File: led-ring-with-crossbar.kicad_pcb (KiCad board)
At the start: 2 copper layers, 99 x 99 mm, 88 parts

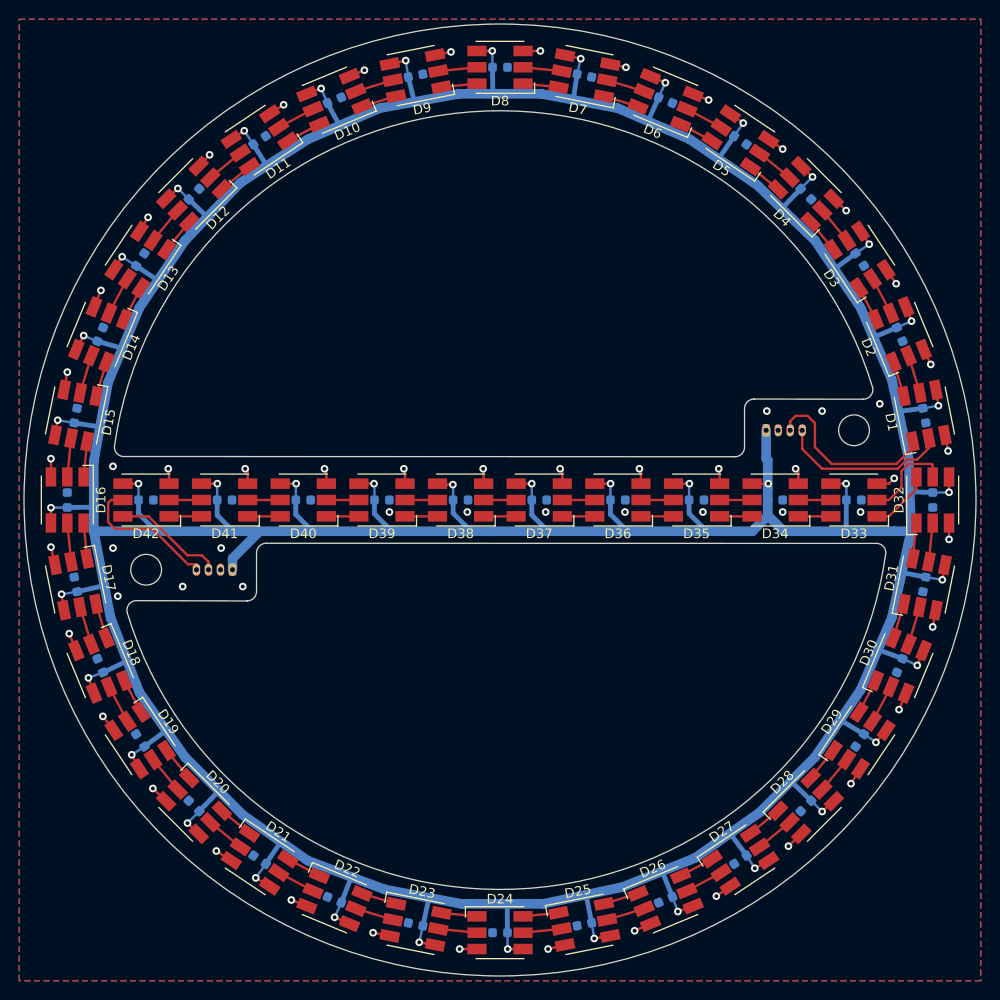
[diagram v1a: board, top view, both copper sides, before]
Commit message: Update to KiCad 6.0
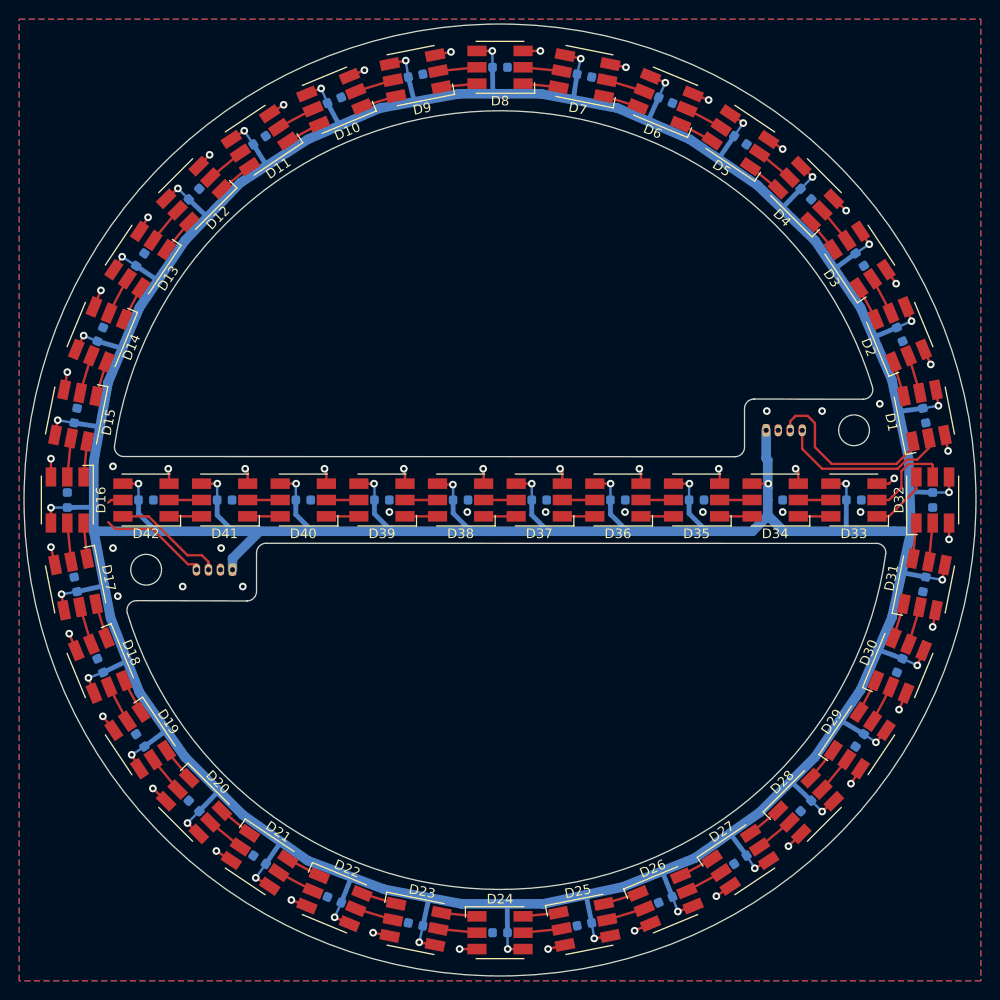
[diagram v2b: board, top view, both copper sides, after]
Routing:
- net COUT: track 15.2 -> 13.2 mm
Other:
- net class Default removed
